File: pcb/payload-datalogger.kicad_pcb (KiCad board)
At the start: 2 copper layers, 43.5 x 41 mm, 42 parts, among them J1 2.54mm 01x02 header, J2 Conn_01x02, J3 Conn_01x02, J4 Conn_01x02, J5 Conn_01x02, SW2 PTS815, U1 XIAO-ESP32-C3-DIP, U2 NCP177AMX330TCG, U3 W25X40CLSN, U4 MCP96RL00T-E_MX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

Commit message: Connect flash decoupling cap to GND
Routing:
- net GND: track 106.6 -> 107.3 mm, vias 16 -> 17
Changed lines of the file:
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@@
+	)
+	(segment
+		(start 106.205 61.905)
+		(end 106.2 61.9)
+		(width 0.5)
+		(layer "F.Cu")
+		(net 2)
 	)
 	(segment
@@
 	)
 	(segment
+		(start 106.975 61.905)
+		(end 106.205 61.905)
+		(width 0.5)
+		(layer "F.Cu")
+		(net 2)
+	)
+	(segment
 		(start 81.3 46.5625)
 		(end 81.3 47.7)
@@
 	(via
 		(at 92 65.3)
+		(size 0.6)
+		(drill 0.3)
+		(layers "F.Cu" "B.Cu")
+		(net 2)
+	)
+	(via
+		(at 106.2 61.9)
 		(size 0.6)
 		(drill 0.3)
@@
 		(min_thickness 0.2)
 		(filled_areas_thickness no)
-		(fill
+		(fill yes
 			(thermal_gap 0.3)
 			(thermal_bridge_width 0.3)
@@
 		(min_thickness 0.2)
 		(filled_areas_thickness no)
-		(fill
+		(fill yes
 			(thermal_gap 0.3)
 			(thermal_bridge_width 0.5)

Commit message: Reroute battery measure
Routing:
- net /BATT_MEAS: track 23.4 -> 28.9 mm, vias 2 -> 0
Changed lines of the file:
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@@
 	)
 	(segment
-		(start 93.5 51.24)
+		(start 93 50)
 		(end 92.26 50)
+		(width 0.2)
+		(layer "F.Cu")
+		(net 4)
+	)
+	(segment
+		(start 95 52)
+		(end 93 50)
 		(width 0.2)
 		(layer "F.Cu")
@@
 	)
 	(segment
-		(start 93.5 68.85)
-		(end 93.5 63.6)
+		(start 95.35 67)
+		(end 97 67)
 		(width 0.2)
 		(layer "F.Cu")
@@
 	)
 	(segment
-		(start 93.5 61.5)
-		(end 93.5 51.24)
+		(start 93.5 68.85)
+		(end 95.35 67)
+		(width 0.2)
+		(layer "F.Cu")
+		(net 4)
+	)
+	(segment
+		(start 98.5 65.5)
+		(end 98.5 61.5)
+		(width 0.2)
+		(layer "F.Cu")
+		(net 4)
+	)
+	(segment
+		(start 98.5 61.5)
+		(end 95 58)
+		(width 0.2)
+		(layer "F.Cu")
+		(net 4)
+	)
+	(segment
+		(start 95 58)
+		(end 95 52)
+		(width 0.2)
+		(layer "F.Cu")
+		(net 4)
+	)
+	(segment
+		(start 97 67)
+		(end 98.5 65.5)
 		(width 0.2)
 		(layer "F.Cu")
@@
 		(net 4)
 	)
-	(via
-		(at 93.5 61.5)
-		(size 0.6)
-		(drill 0.3)
-		(layers "F.Cu" "B.Cu")
-		(net 4)
-	)
-	(via
-		(at 93.5 63.6)
-		(size 0.6)
-		(drill 0.3)
-		(layers "F.Cu" "B.Cu")
-		(net 4)
-	)
-	(segment
-		(start 93.5 63.6)
-		(end 93.5 61.5)
-		(width 0.2)
-		(layer "B.Cu")
-		(net 4)
-	)

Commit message: Tweak battery
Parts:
- moved BT1 1.80 mm to (104.5, 74.5)
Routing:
- net Net-(BT1--): track 6.20 -> 8.00 mm
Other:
- board text added: "BATTERY"
- board text removed: "3.7V"
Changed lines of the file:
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@@
 	(footprint "Connector_JST:JST_PH_B2B-PH-K_1x02_P2.00mm_Vertical"
 		(layer "F.Cu")
-		(at 102.7 74.5 -90)
+		(at 104.5 74.5 -90)
 		(descr "JST PH series connector, B2B-PH-K (http://www.jst-mfg.com/product/pdf/eng/ePH.pdf), generated with kicad-footprint-generator")
 		(tags "connector JST PH side entry")
@@
 	)
 	(gr_text "+ -"
-		(at 106.5 78 90)
+		(at 108.3 78 90)
 		(layer "F.SilkS")
 		(effects
@@
 		)
 	)
-	(gr_text "3.7V"
-		(at 101.5 71.5 0)
+	(gr_text "BATTERY"
+		(at 101 71.5 0)
 		(layer "F.SilkS")
 		(effects
@@
 	)
 	(segment
-		(start 102.7 76.5)
+		(start 104.5 76.5)
 		(end 96.5 76.5)
 		(width 0.5)

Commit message: Update payload-datalogger.kicad_pcb
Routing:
- net +BATT: track 8.52 -> 1.86 mm
- added copper zone on F.Cu, net +BATT
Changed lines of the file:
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@@
 		(start 104.5 76.5)
 		(end 96.5 76.5)
-		(width 0.5)
+		(width 1.2)
 		(layer "F.Cu")
 		(net 1)
@@
 	)
 	(segment
+		(start 97.175 68.925)
+		(end 97.2 68.9)
+		(width 0.5)
+		(layer "F.Cu")
+		(net 2)
+	)
+	(segment
 		(start 106.205 61.905)
 		(end 106.2 61.9)
@@
 	)
 	(segment
+		(start 97.5 69.725)
+		(end 97.175 69.4)
+		(width 0.5)
+		(layer "F.Cu")
+		(net 2)
+	)
+	(segment
 		(start 79.35 57.35)
 		(end 80 58)
@@
 	)
 	(segment
-		(start 97.175 69.4)
-		(end 97.239 69.464)
-		(width 0.5)
-		(layer "F.Cu")
-		(net 2)
-	)
-	(segment
 		(start 80 51.4375)
 		(end 80 50.375)
@@
 	)
 	(segment
-		(start 97.239 69.464)
-		(end 97.239 69.479)
-		(width 0.5)
-		(layer "F.Cu")
-		(net 2)
-	)
-	(segment
 		(start 81.3 65.7)
 		(end 80 67)
@@
 	)
 	(segment
-		(start 97.175 69.24)
-		(end 97.14 69.24)
-		(width 0.5)
-		(layer "F.Cu")
-		(net 2)
-	)
-	(segment
 		(start 79.35 66.35)
 		(end 80 67)
@@
 	)
 	(segment
-		(start 97.175 69.24)
-		(end 97.175 69.4)
-		(width 0.5)
-		(layer "F.Cu")
-		(net 2)
-	)
-	(segment
 		(start 82.4375 49)
 		(end 80 49)
@@
 	)
 	(segment
-		(start 97.14 69.24)
-		(end 96.8 68.9)
-		(width 0.5)
-		(layer "F.Cu")
-		(net 2)
-	)
-	(segment
 		(start 77.5625 47.7)
 		(end 78.7 47.7)
@@
 	)
 	(segment
+		(start 97.175 69.4)
+		(end 97.175 69.24)
+		(width 0.5)
+		(layer "F.Cu")
+		(net 2)
+	)
+	(segment
 		(start 96.500002 64.649998)
 		(end 96.500002 65.299998)
@@
 	)
 	(segment
+		(start 97.175 69.24)
+		(end 97.175 68.925)
+		(width 0.5)
+		(layer "F.Cu")
+		(net 2)
+	)
+	(segment
 		(start 77.5625 68.3)
 		(end 78.55 68.3)
@@
 	)
 	(via
-		(at 96.8 68.9)
-		(size 0.6)
-		(drill 0.3)
-		(layers "F.Cu" "B.Cu")
-		(net 2)
-	)
-	(via
 		(at 102.3 67.8)
 		(size 0.6)
@@
 	(via
 		(at 92 65.3)
+		(size 0.6)
+		(drill 0.3)
+		(layers "F.Cu" "B.Cu")
+		(net 2)
+	)
+	(via
+		(at 97.2 68.9)
 		(size 0.6)
 		(drill 0.3)
@@
 	)
 	(segment
-		(start 96.5 71.5)
-		(end 95.5 70.5)
-		(width 0.5)
+		(start 97.175 70.21)
+		(end 97.175 70.675)
+		(width 0.3)
 		(layer "F.Cu")
 		(net 5)
 	)
 	(segment
-		(start 97 71)
-		(end 97.230508 71)
-		(width 0.5)
+		(start 97.825 70.21)
+		(end 98.29 70.21)
+		(width 0.3)
 		(layer "F.Cu")
 		(net 5)
 	)
 	(segment
-		(start 97 71)
-		(end 97 70.385)
-		(width 0.5)
+		(start 97.8 70.21)
+		(end 97.8 70.675)
+		(width 0.3)
 		(layer "F.Cu")
 		(net 5)
 	)
 	(segment
-		(start 96.5 73.96)
-		(end 96.5 71.5)
-		(width 0.5)
-		(layer "F.Cu")
-		(net 5)
-	)
-	(segment
-		(start 97 70.385)
-		(end 97.077246 70.307754)
-		(width 0.5)
-		(layer "F.Cu")
-		(net 5)
-	)
-	(segment
-		(start 96.5 71.5)
-		(end 97 71)
-		(width 0.5)
-		(layer "F.Cu")
-		(net 5)
-	)
-	(segment
-		(start 97.230508 71)
-		(end 97.922754 70.307754)
-		(width 0.5)
-		(layer "F.Cu")
-		(net 5)
-	)
-	(segment
-		(start 95.5 70.5)
-		(end 93.5 70.5)
-		(width 0.5)
+		(start 97.2 70.21)
+		(end 96.735 70.21)
+		(width 0.3)
 		(layer "F.Cu")
 		(net 5)
@@
 			)
 		)
+	)
+	(zone
+		(net 5)
+		(net_name "+BATT")
+		(layer "F.Cu")
+		(hatch edge 0.5)
+		(priority 2)
+		(connect_pads
+			(clearance 0.2)
+		)
+		(min_thickness 0.2)
+		(filled_areas_thickness no)
+		(fill yes
+			(thermal_gap 0.2)
+			(thermal_bridge_width 0.5)
+		)
+		(polygon
+			(pts
+				(xy 95.3125 75.5) (xy 92.5 71) (xy 92.5 69.7) (xy 98.5 69.7) (xy 98.5 71) (xy 97.9375 75.5)
+			)
+		)

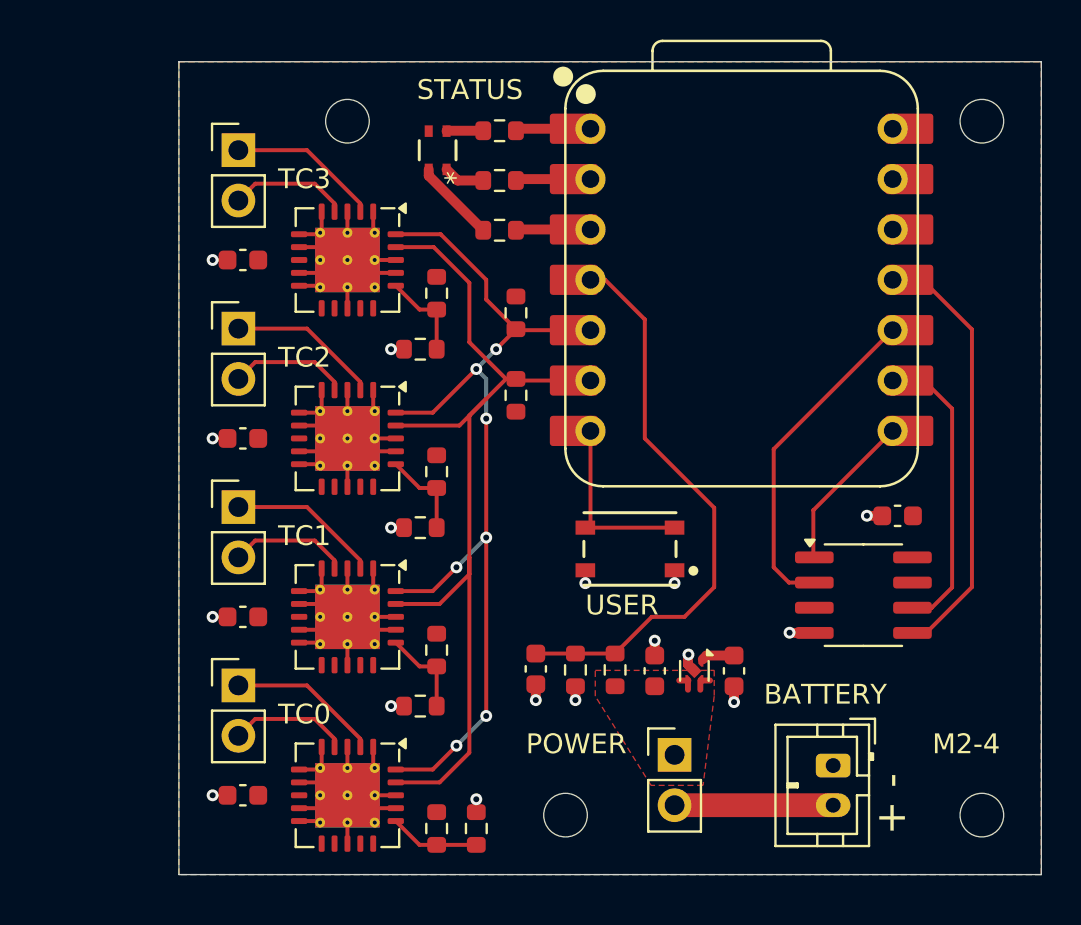
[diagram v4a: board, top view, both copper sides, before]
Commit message: Add rounded corners and 3.3V stitching
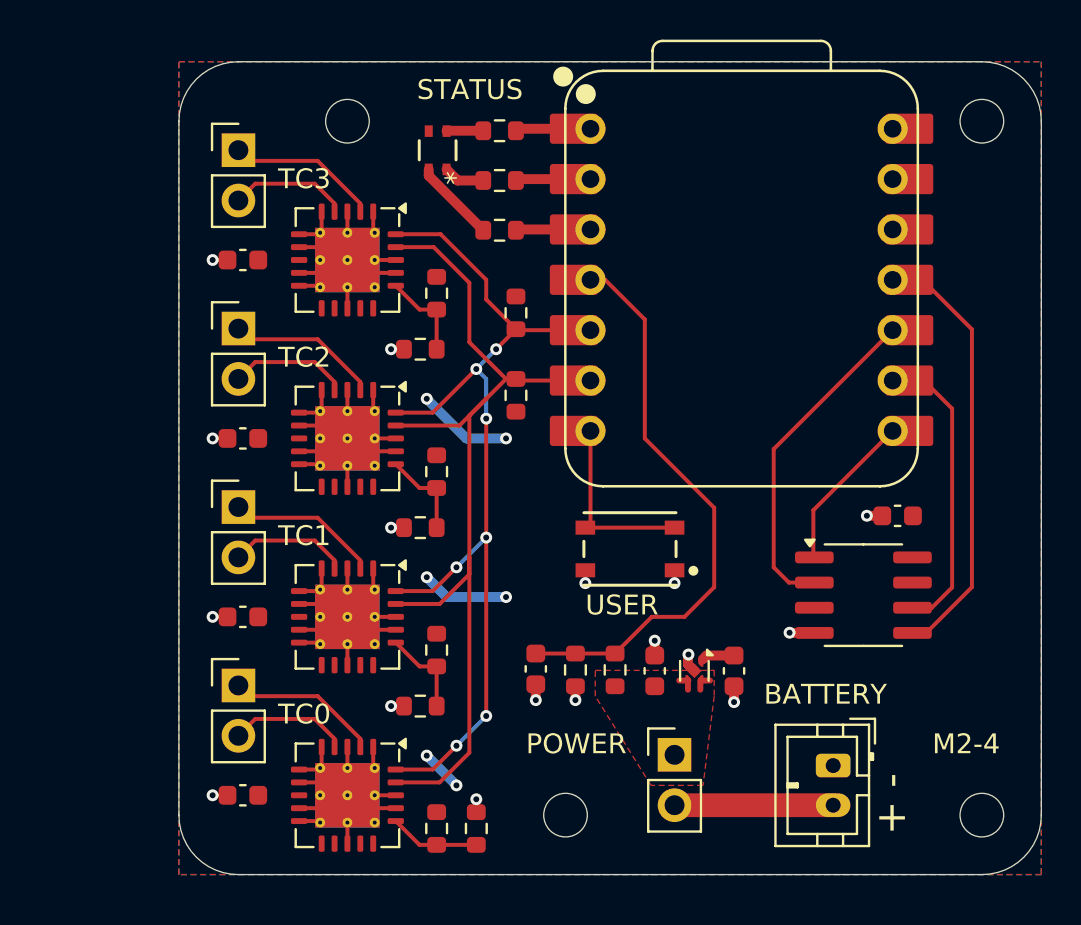
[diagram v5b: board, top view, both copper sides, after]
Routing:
- net +3V3: track 1.66 -> 13.0 mm, vias 0 -> 6
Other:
- outline, holes or cut-outs redrawn
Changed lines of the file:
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@@
 		)
 	)
-	(gr_rect
-		(start 71.5 39)
-		(end 115 80)
+	(gr_line
+		(start 115 42)
+		(end 115 77)
 		(stroke
 			(width 0.05)
 			(type default)
 		)
-		(fill no)
+		(layer "Edge.Cuts")
+	)
+	(gr_line
+		(start 74.5 39)
+		(end 112 39)
+		(stroke
+			(width 0.05)
+			(type default)
+		)
+		(layer "Edge.Cuts")
+	)
+	(gr_arc
+		(start 71.5 42)
+		(mid 72.37868 39.87868)
+		(end 74.5 39)
+		(stroke
+			(width 0.05)
+			(type default)
+		)
+		(layer "Edge.Cuts")
+	)
+	(gr_arc
+		(start 74.5 80)
+		(mid 72.37868 79.12132)
+		(end 71.5 77)
+		(stroke
+			(width 0.05)
+			(type default)
+		)
+		(layer "Edge.Cuts")
+	)
+	(gr_arc
+		(start 115 77)
+		(mid 114.12132 79.12132)
+		(end 112 80)
+		(stroke
+			(width 0.05)
+			(type default)
+		)
+		(layer "Edge.Cuts")
+	)
+	(gr_arc
+		(start 112 39)
+		(mid 114.12132 39.87868)
+		(end 115 42)
+		(stroke
+			(width 0.05)
+			(type default)
+		)
+		(layer "Edge.Cuts")
+	)
+	(gr_line
+		(start 112 80)
+		(end 74.5 80)
+		(stroke
+			(width 0.05)
+			(type default)
+		)
+		(layer "Edge.Cuts")
+	)
+	(gr_line
+		(start 71.5 77)
+		(end 71.5 42)
+		(stroke
+			(width 0.05)
+			(type default)
+		)
 		(layer "Edge.Cuts")
 	)
@@
 		(net 3)
 	)
+	(via
+		(at 88 66)
+		(size 0.6)
+		(drill 0.3)
+		(layers "F.Cu" "B.Cu")
+		(free yes)
+		(net 3)
+	)
+	(via
+		(at 84 56)
+		(size 0.6)
+		(drill 0.3)
+		(layers "F.Cu" "B.Cu")
+		(free yes)
+		(net 3)
+	)
+	(via
+		(at 85.5 75.5)
+		(size 0.6)
+		(drill 0.3)
+		(layers "F.Cu" "B.Cu")
+		(free yes)
+		(net 3)
+	)
+	(via
+		(at 88 58)
+		(size 0.6)
+		(drill 0.3)
+		(layers "F.Cu" "B.Cu")
+		(free yes)
+		(net 3)
+	)
+	(via
+		(at 84 74)
+		(size 0.6)
+		(drill 0.3)
+		(layers "F.Cu" "B.Cu")
+		(free yes)
+		(net 3)
+	)
+	(via
+		(at 84 65)
+		(size 0.6)
+		(drill 0.3)
+		(layers "F.Cu" "B.Cu")
+		(free yes)
+		(net 3)
+	)
+	(segment
+		(start 88 66)
+		(end 85 66)
+		(width 0.5)
+		(layer "B.Cu")
+		(net 3)
+	)
+	(segment
+		(start 85 66)
+		(end 84 65)
+		(width 0.5)
+		(layer "B.Cu")
+		(net 3)
+	)
+	(segment
+		(start 88 58)
+		(end 86 58)
+		(width 0.5)
+		(layer "B.Cu")
+		(net 3)
+	)
+	(segment
+		(start 85.5 75.5)
+		(end 84 74)
+		(width 0.5)
+		(layer "B.Cu")
+		(net 3)
+	)
+	(segment
+		(start 86 58)
+		(end 84 56)
+		(width 0.5)
+		(layer "B.Cu")
+		(net 3)
+	)
 	(segment
 		(start 93 50)
@@
 	)
 	(segment
+		(start 78.499999 71)
+		(end 80.65 73.150001)
+		(width 0.2)
+		(layer "F.Cu")
+		(net 7)
+	)
+	(segment
+		(start 75.04 71)
+		(end 78.499999 71)
+		(width 0.2)
+		(layer "F.Cu")
+		(net 7)
+	)
+	(segment
 		(start 80.65 73.150001)
 		(end 80.65 73.5625)
@@
 	(segment
 		(start 74.5 70.46)
-		(end 77.959999 70.46)
-		(width 0.2)
-		(layer "F.Cu")
-		(net 7)
-	)
-	(segment
-		(start 77.959999 70.46)
-		(end 80.65 73.150001)
+		(end 75.04 71)
 		(width 0.2)
 		(layer "F.Cu")
@@
 	)
 	(segment
-		(start 77.959999 61.46)
-		(end 80.65 64.150001)
+		(start 75.04 62)
+		(end 78.499999 62)
+		(width 0.2)
+		(layer "F.Cu")
+		(net 9)
+	)
+	(segment
+		(start 74.5 61.46)
+		(end 75.04 62)
 		(width 0.2)
 		(layer "F.Cu")
@@
 	)
 	(segment
-		(start 74.5 61.46)
-		(end 77.959999 61.46)
+		(start 78.499999 62)
+		(end 80.65 64.150001)
 		(width 0.2)
 		(layer "F.Cu")
 		(net 9)
+	)
+	(segment
+		(start 78.499999 53)
+		(end 80.65 55.150001)
+		(width 0.2)
+		(layer "F.Cu")
+		(net 10)
+	)
+	(segment
+		(start 75.04 53)
+		(end 78.499999 53)
+		(width 0.2)
+		(layer "F.Cu")
+		(net 10)
 	)
 	(segment
@@
 	(segment
 		(start 74.5 52.46)
-		(end 77.959999 52.46)
-		(width 0.2)
-		(layer "F.Cu")
-		(net 10)
-	)
-	(segment
-		(start 77.959999 52.46)
-		(end 80.65 55.150001)
+		(end 75.04 53)
 		(width 0.2)
 		(layer "F.Cu")
@@
 	)
 	(segment
+		(start 75.04 44)
+		(end 78.499999 44)
+		(width 0.2)
+		(layer "F.Cu")
+		(net 33)
+	)
+	(segment
+		(start 78.499999 44)
+		(end 80.65 46.150001)
+		(width 0.2)
+		(layer "F.Cu")
+		(net 33)
+	)
+	(segment
 		(start 74.5 43.46)
-		(end 77.959999 43.46)
-		(width 0.2)
-		(layer "F.Cu")
-		(net 33)
-	)
-	(segment
-		(start 77.959999 43.46)
-		(end 80.65 46.150001)
-		(width 0.2)
-		(layer "F.Cu")
+		(end 75.04 44)
+		(width 0.2)
+		(layer "F.Cu")

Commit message: Update payload-datalogger.kicad_pcb
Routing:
- net GND: track 107.5 -> 131.5 mm, vias 17 -> 53
- net +3V3: track 13.0 -> 18.5 mm

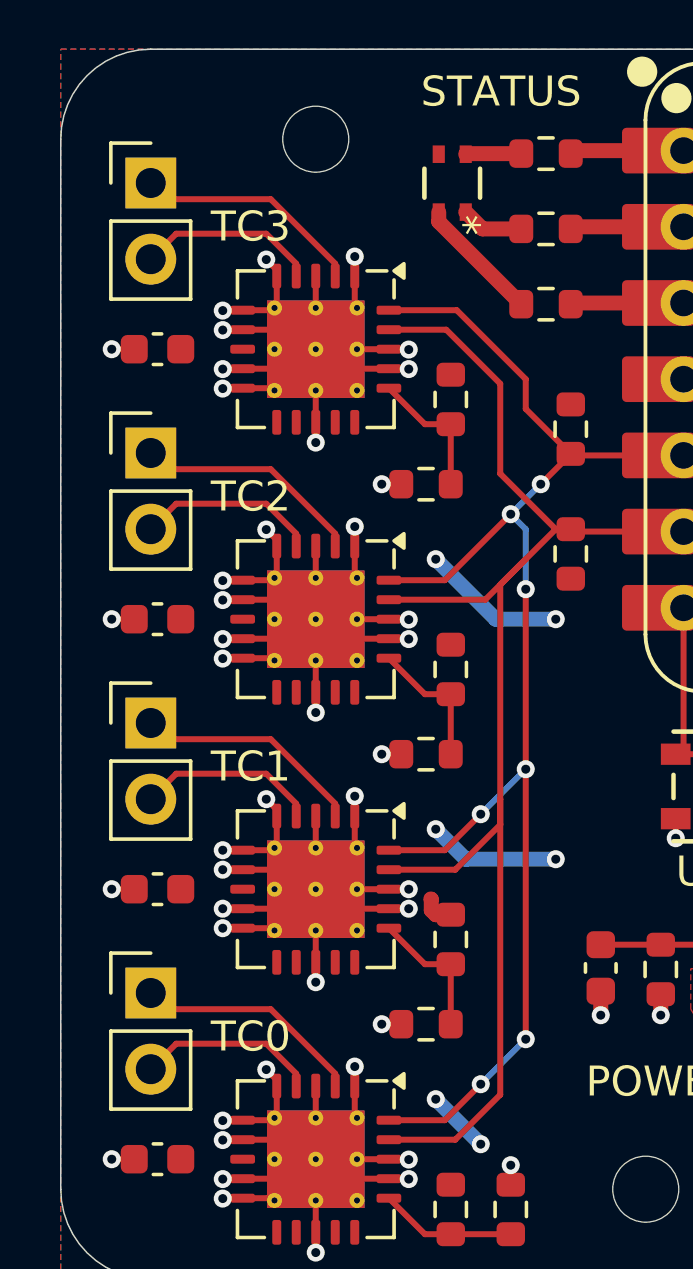
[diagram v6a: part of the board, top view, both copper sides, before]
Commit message: Update schematic for DE15
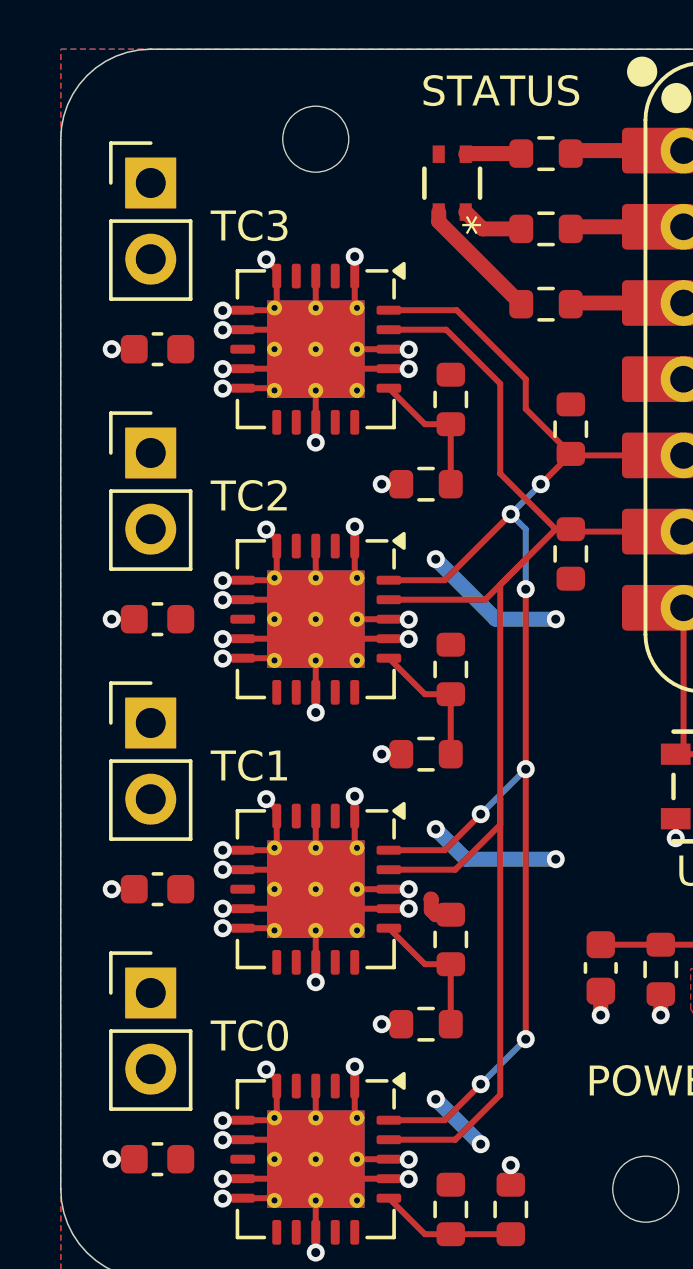
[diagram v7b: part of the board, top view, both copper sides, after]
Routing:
- net Net-(J2-Pin_1): track 7.68 -> 0.00 mm
- net Net-(J5-Pin_1): track 7.68 -> 0.00 mm
- net Net-(J4-Pin_1): track 7.68 -> 0.00 mm
- net Net-(J3-Pin_1): track 7.68 -> 0.00 mm
- net Net-(J5-Pin_2): track 6.03 -> 0.00 mm
- net Net-(J4-Pin_2): track 6.03 -> 0.00 mm
- net Net-(J3-Pin_2): track 6.03 -> 0.00 mm
- net Net-(J2-Pin_2): track 6.03 -> 0.00 mm
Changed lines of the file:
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@@
-	)
-	(segment
-		(start 79.35 73.150001)
-		(end 79.35 73.5625)
-		(width 0.2)
-		(layer "F.Cu")
-		(net 6)
-	)
-	(segment
-		(start 74.5 73)
-		(end 75.35 72.15)
-		(width 0.2)
-		(layer "F.Cu")
-		(net 6)
-	)
-	(segment
-		(start 75.35 72.15)
-		(end 78.349999 72.15)
-		(width 0.2)
-		(layer "F.Cu")
-		(net 6)
-	)
-	(segment
-		(start 78.349999 72.15)
-		(end 79.35 73.150001)
-		(width 0.2)
-		(layer "F.Cu")
-		(net 6)
-	)
-	(segment
-		(start 78.499999 71)
-		(end 80.65 73.150001)
-		(width 0.2)
-		(layer "F.Cu")
-		(net 7)
-	)
-	(segment
-		(start 75.04 71)
-		(end 78.499999 71)
-		(width 0.2)
-		(layer "F.Cu")
-		(net 7)
-	)
-	(segment
-		(start 80.65 73.150001)
-		(end 80.65 73.5625)
-		(width 0.2)
-		(layer "F.Cu")
-		(net 7)
-	)
-	(segment
-		(start 74.5 70.46)
-		(end 75.04 71)
-		(width 0.2)
-		(layer "F.Cu")
-		(net 7)
-	)
-	(segment
-		(start 75.35 63.15)
-		(end 78.349999 63.15)
-		(width 0.2)
-		(layer "F.Cu")
-		(net 8)
-	)
-	(segment
-		(start 74.5 64)
-		(end 75.35 63.15)
-		(width 0.2)
-		(layer "F.Cu")
-		(net 8)
-	)
-	(segment
-		(start 79.35 64.150001)
-		(end 79.35 64.5625)
-		(width 0.2)
-		(layer "F.Cu")
-		(net 8)
-	)
-	(segment
-		(start 78.349999 63.15)
-		(end 79.35 64.150001)
-		(width 0.2)
-		(layer "F.Cu")
-		(net 8)
-	)
-	(segment
-		(start 75.04 62)
-		(end 78.499999 62)
-		(width 0.2)
-		(layer "F.Cu")
-		(net 9)
-	)
-	(segment
-		(start 74.5 61.46)
-		(end 75.04 62)
-		(width 0.2)
-		(layer "F.Cu")
-		(net 9)
-	)
-	(segment
-		(start 80.65 64.150001)
-		(end 80.65 64.5625)
-		(width 0.2)
-		(layer "F.Cu")
-		(net 9)
-	)
-	(segment
-		(start 78.499999 62)
-		(end 80.65 64.150001)
-		(width 0.2)
-		(layer "F.Cu")
-		(net 9)
-	)
-	(segment
-		(start 78.499999 53)
-		(end 80.65 55.150001)
-		(width 0.2)
-		(layer "F.Cu")
-		(net 10)
-	)
-	(segment
-		(start 75.04 53)
-		(end 78.499999 53)
-		(width 0.2)
-		(layer "F.Cu")
-		(net 10)
-	)
-	(segment
-		(start 80.65 55.150001)
-		(end 80.65 55.5625)
-		(width 0.2)
-		(layer "F.Cu")
-		(net 10)
-	)
-	(segment
-		(start 74.5 52.46)
-		(end 75.04 53)
-		(width 0.2)
-		(layer "F.Cu")
-		(net 10)
-	)
-	(segment
-		(start 79.35 55.150001)
-		(end 79.35 55.5625)
-		(width 0.2)
-		(layer "F.Cu")
-		(net 11)
-	)
-	(segment
-		(start 78.349999 54.15)
-		(end 79.35 55.150001)
-		(width 0.2)
-		(layer "F.Cu")
-		(net 11)
-	)
-	(segment
-		(start 75.35 54.15)
-		(end 78.349999 54.15)
-		(width 0.2)
-		(layer "F.Cu")
-		(net 11)
-	)
-	(segment
-		(start 74.5 55)
-		(end 75.35 54.15)
-		(width 0.2)
-		(layer "F.Cu")
-		(net 11)
 	)
 	(segment
@@
 	)
 	(segment
-		(start 75.04 44)
-		(end 78.499999 44)
-		(width 0.2)
-		(layer "F.Cu")
-		(net 33)
-	)
-	(segment
-		(start 78.499999 44)
-		(end 80.65 46.150001)
-		(width 0.2)
-		(layer "F.Cu")
-		(net 33)
-	)
-	(segment
-		(start 74.5 43.46)
-		(end 75.04 44)
-		(width 0.2)
-		(layer "F.Cu")
-		(net 33)
-	)
-	(segment
-		(start 80.65 46.150001)
-		(end 80.65 46.5625)
-		(width 0.2)
-		(layer "F.Cu")
-		(net 33)
-	)
-	(segment
-		(start 74.5 46)
-		(end 75.35 45.15)
-		(width 0.2)
-		(layer "F.Cu")
-		(net 34)
-	)
-	(segment
-		(start 75.35 45.15)
-		(end 78.349999 45.15)
-		(width 0.2)
-		(layer "F.Cu")
-		(net 34)
-	)
-	(segment
-		(start 78.349999 45.15)
-		(end 79.35 46.150001)
-		(width 0.2)
-		(layer "F.Cu")
-		(net 34)
-	)
-	(segment
-		(start 79.35 46.150001)
-		(end 79.35 46.5625)
-		(width 0.2)
-		(layer "F.Cu")
-		(net 34)
-	)
-	(segment
